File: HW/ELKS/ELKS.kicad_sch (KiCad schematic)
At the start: 4 parts, among them U1 ESP32-S3

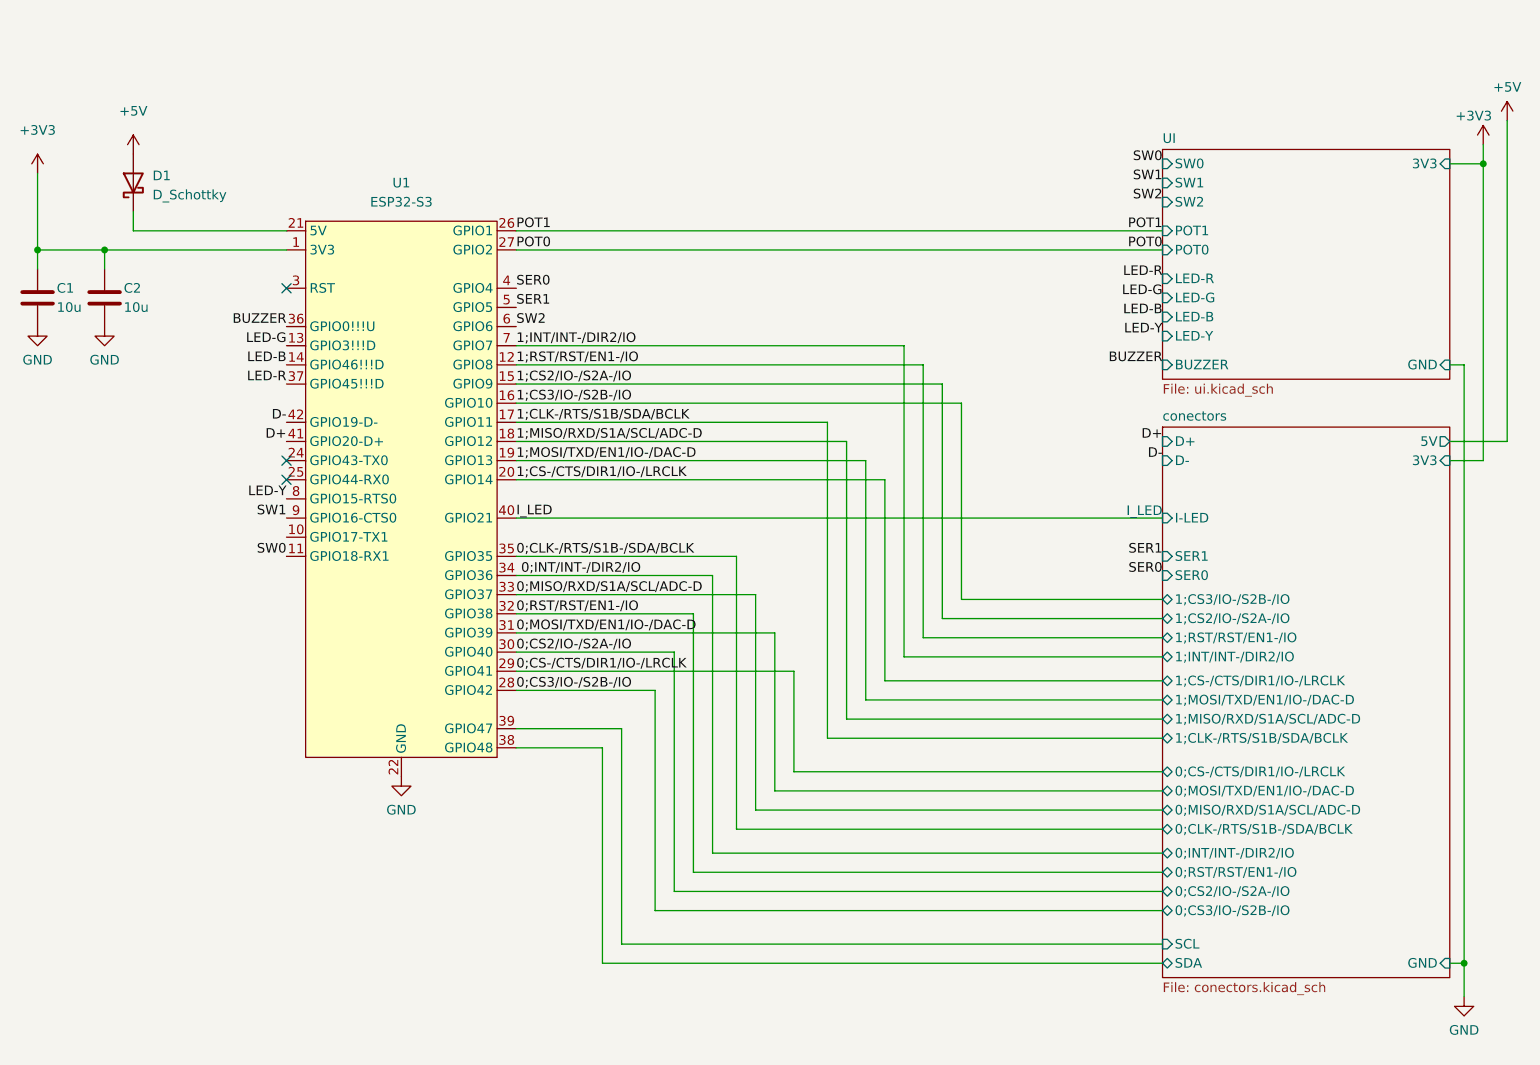
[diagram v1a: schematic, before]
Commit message: Devkit pin headers, ADC to PMODs connectors, moving buttons and LEDs
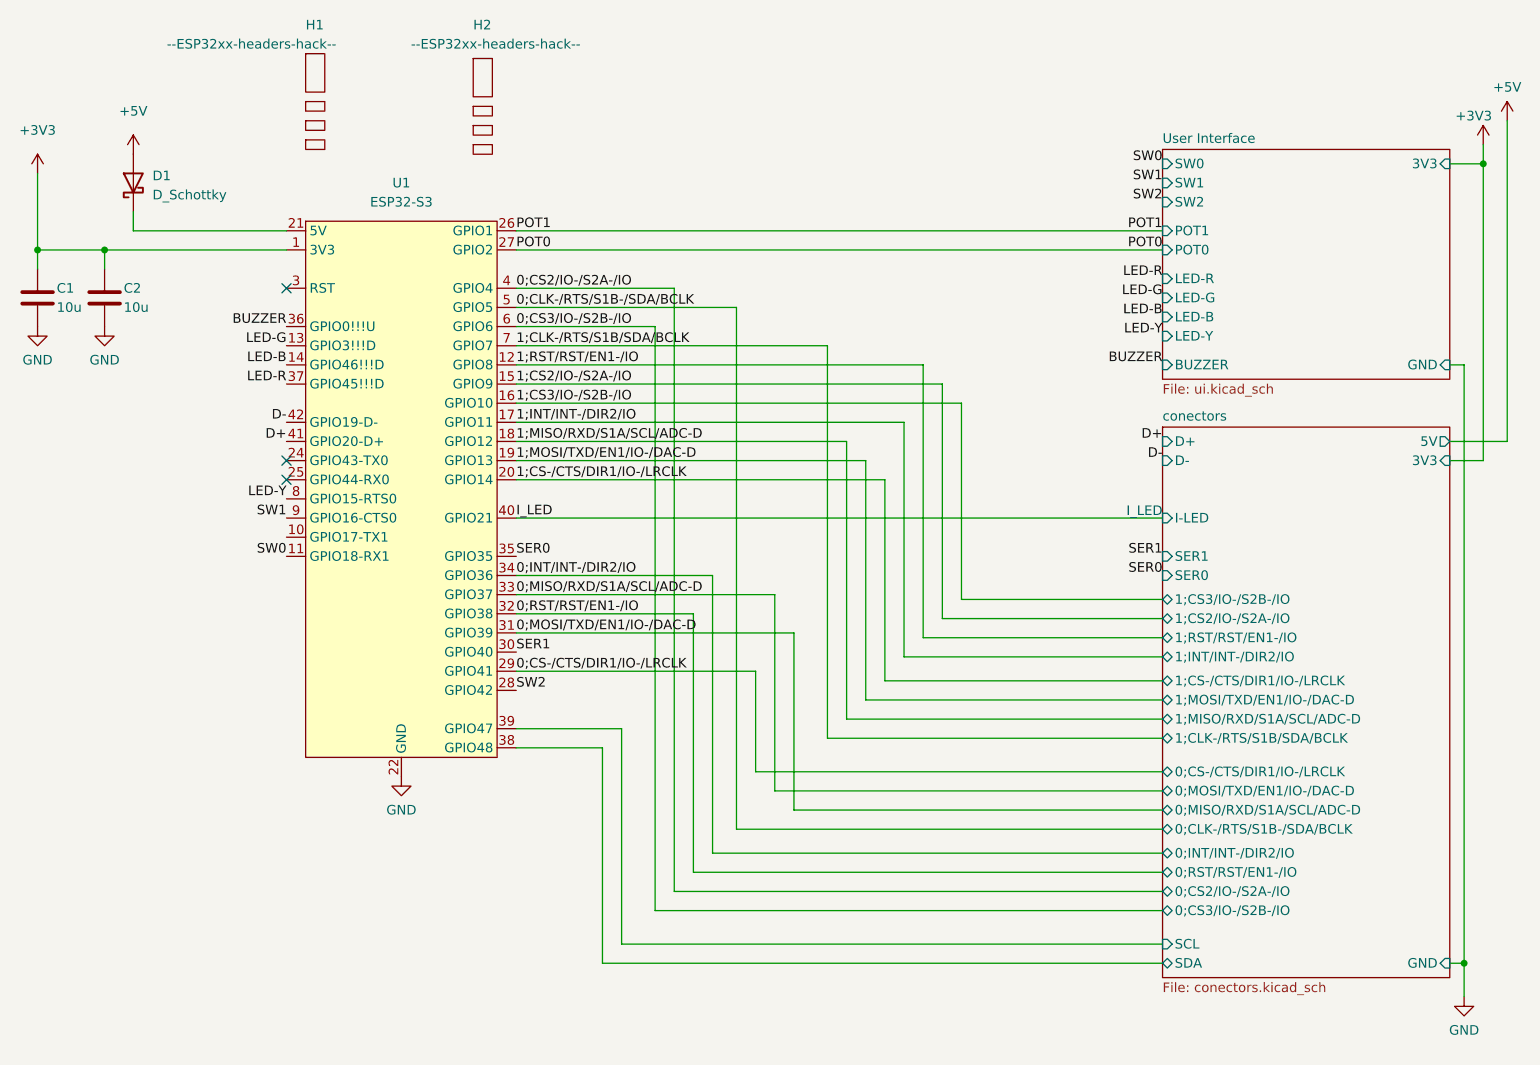
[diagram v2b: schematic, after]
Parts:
- added H1, H2: --ESP32xx-headers-hack--, Robotarna_KiCad_Library:--ESP32xx-headers-hack--, symbol Robotarna_KiCad_Library:--ESP32xx-headers-hack--
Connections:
- net 0;CLK-/RTS/S1B-/SDA/BCLK: now also U1.5 (GPIO5); no longer U1.35 (GPIO35)
- net 0;CS2/IO-/S2A-/IO: now also U1.4 (GPIO4); no longer U1.30 (GPIO40)
- net 0;CS3/IO-/S2B-/IO: now also U1.6 (GPIO6); no longer U1.28 (GPIO42)
- net 1;CLK-/RTS/S1B/SDA/BCLK: now also U1.7 (GPIO7); no longer U1.17 (GPIO11)
- net 1;INT/INT-/DIR2/IO: now also U1.17 (GPIO11); no longer U1.7 (GPIO7)
- net SER0: now also U1.35 (GPIO35); no longer U1.4 (GPIO4)
- net SER1: now also U1.30 (GPIO40); no longer U1.5 (GPIO5)
- net SW2: now also U1.28 (GPIO42); no longer U1.6 (GPIO6)
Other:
- sheet UI renamed User Interface

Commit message: Buzzer connected directly to ESP, UES diodes
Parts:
- removed D1: D_Schottky, Diode_SMD:D_SMA, symbol Device:D_Schottky
- H2: LCSC (none) -> C2886702
- U1: JLCPCB_IGNORE (none) -> 1
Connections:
- net +5V: now also U1.21 (5V)
- net LED-G: now also U1.10 (GPIO17-TX1); no longer U1.13 (GPIO3!!!D)
- net BUZZER renamed BUZZER+
- new net BUZZER-: U1.13 (GPIO3!!!D)
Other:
- sheet User Interface ports: added BUZZER+, BUZZER-; removed BUZZER
